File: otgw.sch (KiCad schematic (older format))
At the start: 37 parts, among them CON1 BARREL_JACK, P2 CONN_01X05, P3 CONN_01X03, P4 CONN_01X02, P5 CONN_01X02, P6 MYSX_2.0, P7 CONN_01X06, Q1 BC558, Q2 BC558, Q3 BC558, Q4 BC547, Q5 BC558, U1 PIC16(L)F88-I/P, U2 PC827, U3 7805

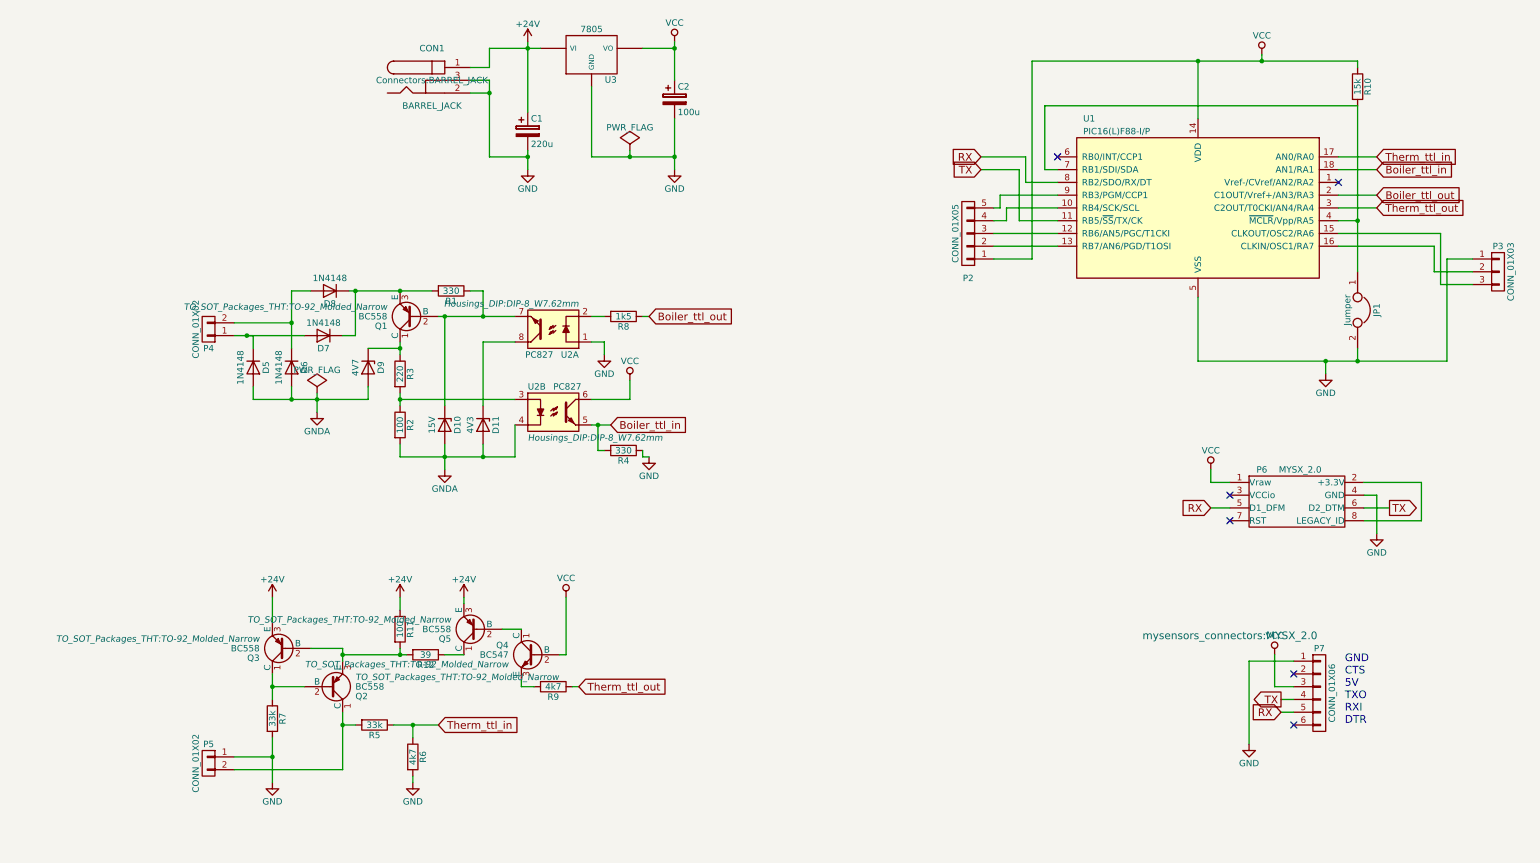
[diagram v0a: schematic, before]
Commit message: Annotations on the schematic and some small Silkscreen additions
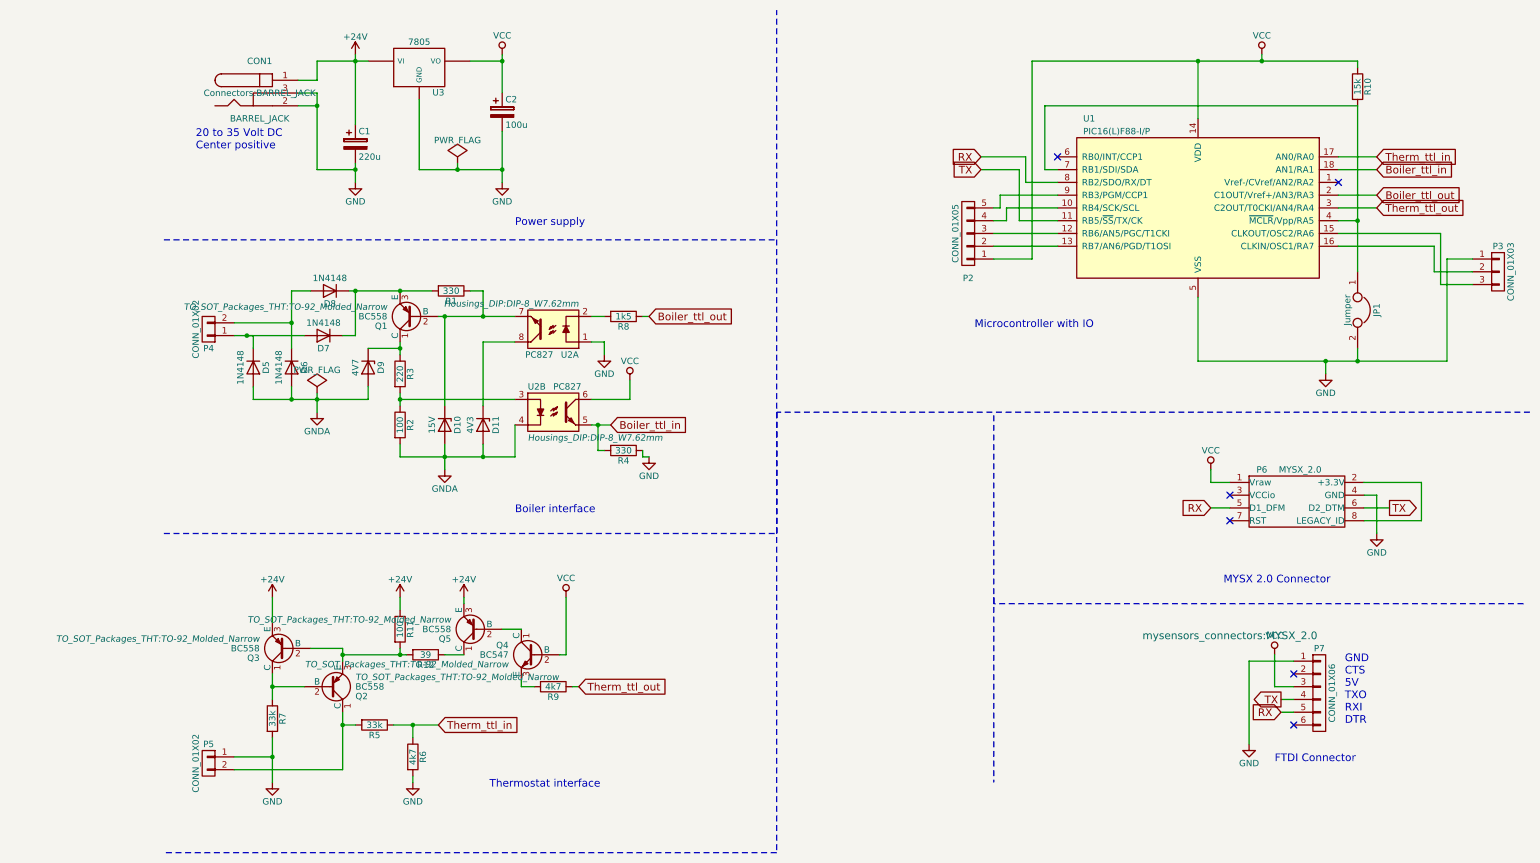
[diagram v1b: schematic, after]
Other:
- note added: "20 to 35 Volt DC\nCenter positive"
- note added: "Boiler interface"
- note added: "FTDI Connector"
- note added: "MYSX 2.0 Connector"
- note added: "Microcontroller with IO"
- note added: "Power supply"
- note added: "Thermostat interface"
- moved on the sheet: C1, C2, CON1, U3
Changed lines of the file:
@@
 encoding utf-8
 Sheet 1 1
-Title ""
-Date ""
-Rev ""
-Comp ""
+Title "Mysensors opentherm gateway"
+Date "2017-06-19"
+Rev "0"
+Comp "pythsoft"
 Comment1 ""
 Comment2 ""
@@
 L CP C1
 U 1 1 59414415
-P 3350 1450
-F 0 "C1" H 3375 1550 50  0000 L CNN
-F 1 "220u" H 3375 1350 50  0000 L CNN
-F 2 "Capacitors_THT:CP_Radial_D10.0mm_P5.00mm_P7.50mm" H 3388 1300 50  0001 C CNN
-F 3 "" H 3350 1450 50  0000 C CNN
-	1    3350 1450
+P 2000 1550
+F 0 "C1" H 2025 1650 50  0000 L CNN
+F 1 "220u" H 2025 1450 50  0000 L CNN
+F 2 "Capacitors_THT:CP_Radial_D10.0mm_P5.00mm_P7.50mm" H 2038 1400 50  0001 C CNN
+F 3 "" H 2000 1550 50  0000 C CNN
+	1    2000 1550
 	1    0    0    -1
 $EndComp
@@
 L 7805 U3
 U 1 1 5941443C
-P 3850 850
-F 0 "U3" H 4000 654 50  0000 C CNN
-F 1 "7805" H 3850 1050 50  0000 C CNN
-F 2 "TO_SOT_Packages_THT:TO-220_Vertical" H 3850 850 50  0001 C CNN
-F 3 "" H 3850 850 50  0000 C CNN
-	1    3850 850
+P 2500 950
+F 0 "U3" H 2650 754 50  0000 C CNN
+F 1 "7805" H 2500 1150 50  0000 C CNN
+F 2 "TO_SOT_Packages_THT:TO-220_Vertical" H 2500 950 50  0001 C CNN
+F 3 "" H 2500 950 50  0000 C CNN
+	1    2500 950
 	1    0    0    -1
 $EndComp
@@
 L CP C2
 U 1 1 5941446D
-P 4500 1200
-F 0 "C2" H 4525 1300 50  0000 L CNN
-F 1 "100u" H 4525 1100 50  0000 L CNN
-F 2 "Capacitors_THT:CP_Radial_D10.0mm_P5.00mm_P7.50mm" H 4538 1050 50  0001 C CNN
-F 3 "" H 4500 1200 50  0000 C CNN
-	1    4500 1200
+P 3150 1300
+F 0 "C2" H 3175 1400 50  0000 L CNN
+F 1 "100u" H 3175 1200 50  0000 L CNN
+F 2 "Capacitors_THT:CP_Radial_D10.0mm_P5.00mm_P7.50mm" H 3188 1150 50  0001 C CNN
+F 3 "" H 3150 1300 50  0000 C CNN
+	1    3150 1300
 	1    0    0    -1
 $EndComp
@@
 L GND #PWR01
 U 1 1 594144F9
-P 4500 1750
-F 0 "#PWR01" H 4500 1500 50  0001 C CNN
-F 1 "GND" H 4500 1600 50  0000 C CNN
-F 2 "" H 4500 1750 50  0000 C CNN
-F 3 "" H 4500 1750 50  0000 C CNN
-	1    4500 1750
+P 3150 1850
+F 0 "#PWR01" H 3150 1600 50  0001 C CNN
+F 1 "GND" H 3150 1700 50  0000 C CNN
+F 2 "" H 3150 1850 50  0000 C CNN
+F 3 "" H 3150 1850 50  0000 C CNN
+	1    3150 1850
 	1    0    0    -1
 $EndComp
@@
 L VCC #PWR02
 U 1 1 59414523
-P 4500 750
-F 0 "#PWR02" H 4500 600 50  0001 C CNN
-F 1 "VCC" H 4500 900 50  0000 C CNN
-F 2 "" H 4500 750 50  0000 C CNN
-F 3 "" H 4500 750 50  0000 C CNN
-	1    4500 750
+P 3150 850
+F 0 "#PWR02" H 3150 700 50  0001 C CNN
+F 1 "VCC" H 3150 1000 50  0000 C CNN
+F 2 "" H 3150 850 50  0000 C CNN
+F 3 "" H 3150 850 50  0000 C CNN
+	1    3150 850
 	1    0    0    -1
 $EndComp
@@
 L +24V #PWR03
 U 1 1 5941454D
-P 3350 750
-F 0 "#PWR03" H 3350 600 50  0001 C CNN
-F 1 "+24V" H 3350 890 50  0000 C CNN
-F 2 "" H 3350 750 50  0000 C CNN
-F 3 "" H 3350 750 50  0000 C CNN
-	1    3350 750
-	1    0    0    -1
-$EndComp
-Wire Wire Line
-	3350 750  3350 1300
-Connection ~ 3350 800
-Wire Wire Line
-	3350 1600 3350 1750
-Wire Wire Line
-	3850 1100 3850 1650
-Wire Wire Line
-	3850 1650 4500 1650
-Wire Wire Line
-	4500 1350 4500 1750
-Connection ~ 4500 1650
-Wire Wire Line
-	4500 750  4500 1050
-Wire Wire Line
-	4250 800  4500 800
-Connection ~ 4500 800
+P 2000 850
+F 0 "#PWR03" H 2000 700 50  0001 C CNN
+F 1 "+24V" H 2000 990 50  0000 C CNN
+F 2 "" H 2000 850 50  0000 C CNN
+F 3 "" H 2000 850 50  0000 C CNN
+	1    2000 850
+	1    0    0    -1
+$EndComp
+Wire Wire Line
+	2000 850  2000 1400
+Connection ~ 2000 900
+Wire Wire Line
+	2000 1700 2000 1850
+Wire Wire Line
+	2500 1200 2500 1750
+Wire Wire Line
+	2500 1750 3150 1750
+Wire Wire Line
+	3150 1450 3150 1850
+Connection ~ 3150 1750
+Wire Wire Line
+	3150 850  3150 1150
+Wire Wire Line
+	2900 900  3150 900
+Connection ~ 3150 900
 $Comp
 L PIC16(L)F88-I/P U1
@@
 L PWR_FLAG #FLG022
 U 1 1 59429FF5
-P 4150 1600
-F 0 "#FLG022" H 4150 1695 50  0001 C CNN
-F 1 "PWR_FLAG" H 4150 1780 50  0000 C CNN
-F 2 "" H 4150 1600 50  0000 C CNN
-F 3 "" H 4150 1600 50  0000 C CNN
-	1    4150 1600
-	1    0    0    -1
-$EndComp
-Wire Wire Line
-	4150 1600 4150 1650
-Connection ~ 4150 1650
+P 2800 1700
+F 0 "#FLG022" H 2800 1795 50  0001 C CNN
+F 1 "PWR_FLAG" H 2800 1880 50  0000 C CNN
+F 2 "" H 2800 1700 50  0000 C CNN
+F 3 "" H 2800 1700 50  0000 C CNN
+	1    2800 1700
+	1    0    0    -1
+$EndComp
+Wire Wire Line
+	2800 1700 2800 1750
+Connection ~ 2800 1750
 $Comp
 L BARREL_JACK CON1
 U 1 1 594294D4
-P 2600 1050
-F 0 "CON1" H 2600 1300 50  0000 C CNN
-F 1 "BARREL_JACK" H 2600 850 50  0000 C CNN
-F 2 "Connectors:BARREL_JACK" H 2600 1050 50  0000 C CNN
-F 3 "" H 2600 1050 50  0000 C CNN
-	1    2600 1050
-	1    0    0    -1
-$EndComp
-Wire Wire Line
-	2900 950  3050 950
-Wire Wire Line
-	3050 950  3050 800
-Wire Wire Line
-	3050 800  3450 800
-Wire Wire Line
-	3050 1650 3350 1650
-Wire Wire Line
-	3050 1050 3050 1650
-Wire Wire Line
-	3050 1150 2900 1150
-Wire Wire Line
-	2900 1050 3050 1050
-Connection ~ 3050 1150
+P 1250 1150
+F 0 "CON1" H 1250 1400 50  0000 C CNN
+F 1 "BARREL_JACK" H 1250 950 50  0000 C CNN
+F 2 "Connectors:BARREL_JACK" H 1250 1150 50  0000 C CNN
+F 3 "" H 1250 1150 50  0000 C CNN
+	1    1250 1150
+	1    0    0    -1
+$EndComp
+Wire Wire Line
+	1550 1050 1700 1050
+Wire Wire Line
+	1700 1050 1700 900
+Wire Wire Line
+	1700 900  2100 900
+Wire Wire Line
+	1700 1750 2000 1750
+Wire Wire Line
+	1700 1150 1700 1750
+Wire Wire Line
+	1700 1250 1550 1250
+Wire Wire Line
+	1550 1150 1700 1150
+Connection ~ 1700 1250
 $Comp
 L GND #PWR023
 U 1 1 59429864
-P 3350 1750
-F 0 "#PWR023" H 3350 1500 50  0001 C CNN
-F 1 "GND" H 3350 1600 50  0000 C CNN
-F 2 "" H 3350 1750 50  0000 C CNN
-F 3 "" H 3350 1750 50  0000 C CNN
-	1    3350 1750
-	1    0    0    -1
-$EndComp
-Connection ~ 3350 1650
+P 2000 1850
+F 0 "#PWR023" H 2000 1600 50  0001 C CNN
+F 1 "GND" H 2000 1700 50  0000 C CNN
+F 2 "" H 2000 1850 50  0000 C CNN
+F 3 "" H 2000 1850 50  0000 C CNN
+	1    2000 1850
+	1    0    0    -1
+$EndComp
+Connection ~ 2000 1750
+Wire Notes Line
+	500  4600 5300 4600
+Wire Notes Line
+	5300 4600 5300 500
+Wire Notes Line
+	500  2300 5300 2300
+Wire Notes Line
+	11200 3650 5300 3650
+Wire Notes Line
+	5300 3650 5300 7100
+Wire Notes Line
+	7000 5100 7000 6550
+Wire Notes Line
+	5300 7100 500  7100
+Text Notes 8800 5000 0    60   ~ 0
+MYSX 2.0 Connector
+Text Notes 9200 6400 0    60   ~ 0
+FTDI Connector
+Text Notes 3050 6600 0    60   ~ 0
+Thermostat interface
+Text Notes 3250 4450 0    60   ~ 0
+Boiler interface
+Text Notes 3250 2200 0    60   ~ 0
+Power supply
+Text Notes 750  1600 0    60   ~ 0
+20 to 35 Volt DC\nCenter positive
+Text Notes 6850 3000 0    60   ~ 0
+Microcontroller with IO
+Wire Notes Line
+	11150 5150 7000 5150
+Wire Notes Line
+	7000 5150 7000 3650
 $EndSCHEMATC
